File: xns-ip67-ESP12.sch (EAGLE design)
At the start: 86 parts, among them J1 DCJ0202

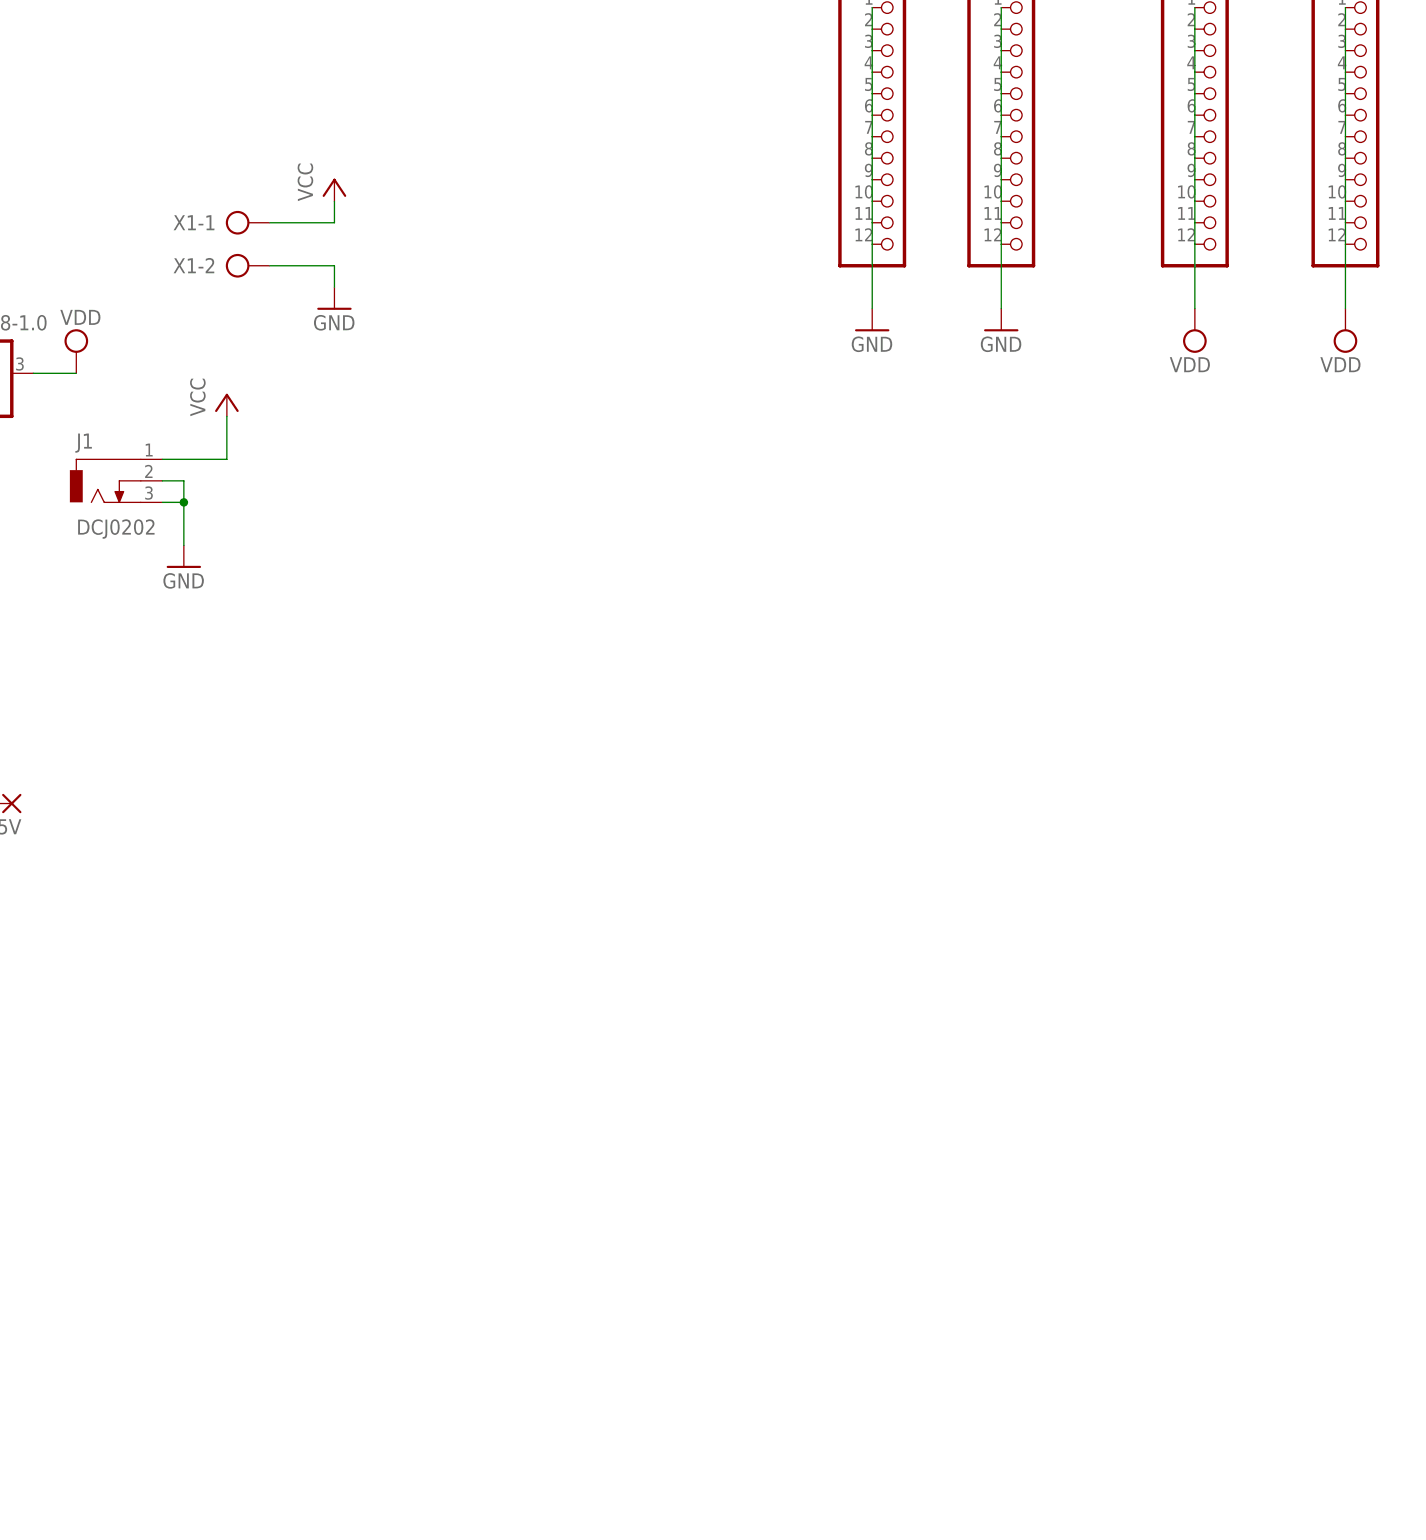
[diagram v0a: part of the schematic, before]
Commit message: Updated design
Added more wire pads on side of ESP
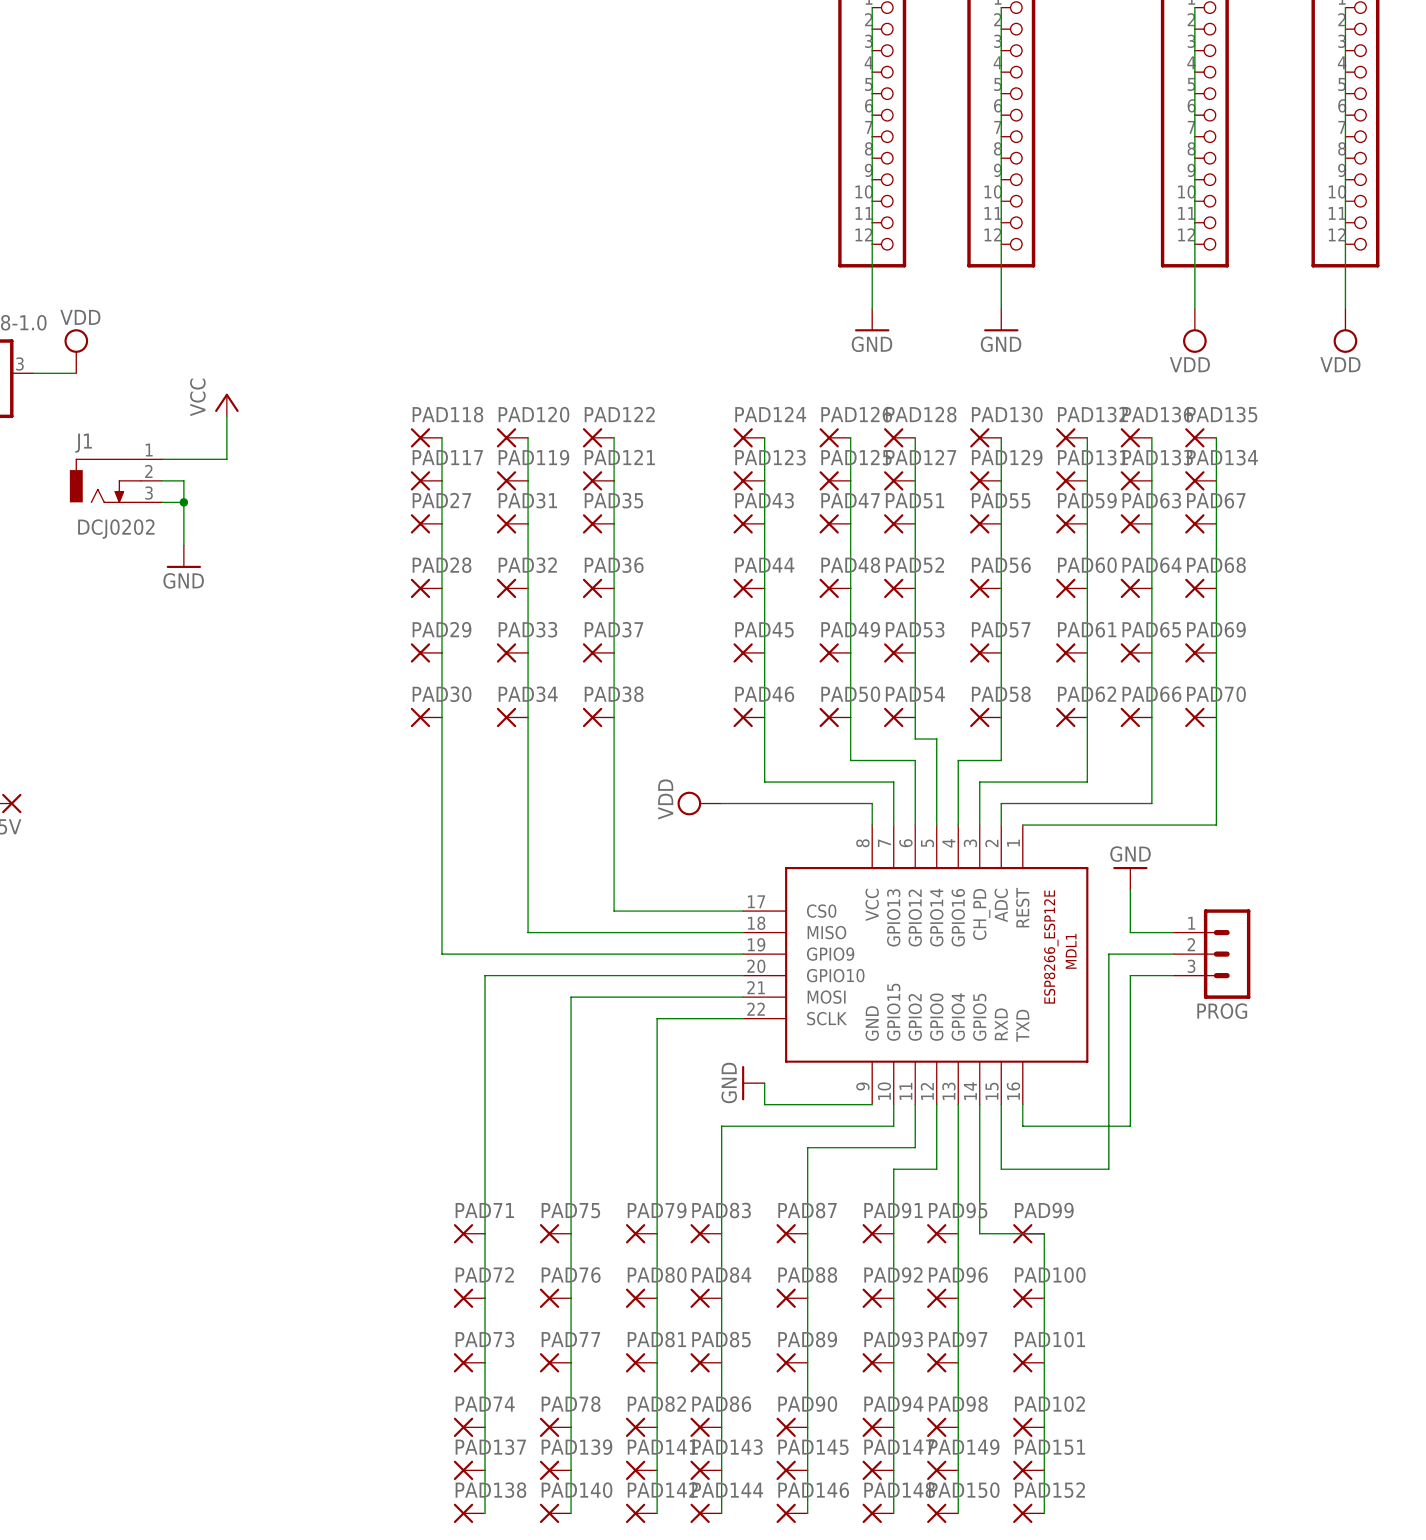
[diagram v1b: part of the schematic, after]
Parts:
- removed X1: (no value), con-ptr500:AK300/2
- added MDL1: (no value), ESP8266-ESP12E:ESP8266-12EESP8266-ESP12E
- added PAD100, PAD101, PAD102, PAD117, PAD118, PAD119, PAD120, PAD121, PAD122, PAD123, PAD124, PAD125, PAD126, PAD127, PAD128, PAD129, PAD130, PAD131, PAD132, PAD133, PAD134, PAD135, PAD136, PAD137, PAD138, PAD139, PAD140, PAD141, PAD142, PAD143, PAD144, PAD145, PAD146, PAD147, PAD148, PAD149, PAD150, PAD151, PAD152, PAD27, PAD28, PAD29, PAD30, PAD31, PAD32, PAD33, PAD34, PAD35, PAD36, PAD37, PAD38, PAD43, PAD44, PAD45, PAD46, PAD47, PAD48, PAD49, PAD50, PAD51, PAD52, PAD53, PAD54, PAD55, PAD56, PAD57, PAD58, PAD59, PAD60, PAD61, PAD62, PAD63, PAD64, PAD65, PAD66, PAD67, PAD68, PAD69, PAD70, PAD71, PAD72, PAD73, PAD74, PAD75, PAD76, PAD77, PAD78, PAD79, PAD80, PAD81, PAD82, PAD83, PAD84, PAD85, PAD86, PAD87, PAD88, PAD89, PAD90, PAD91, PAD92, PAD93, PAD94, PAD95, PAD96, PAD97, PAD98, PAD99: WIREPAD1,6/0,9, wirepad:WIREPAD1,6/0,9
- added PROG: (no value), con-lstb:MA03-1
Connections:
- new net N$1: MDL1.GPIO9, PAD117.P, PAD118.P, PAD27.P, PAD28.P, PAD29.P, PAD30.P
- new net N$10: MDL1.ADC, PAD133.P, PAD136.P, PAD63.P, PAD64.P, PAD65.P, PAD66.P
- new net N$11: MDL1.REST, PAD134.P, PAD135.P, PAD67.P, PAD68.P, PAD69.P, PAD70.P
- new net N$12: MDL1.GPIO10, PAD137.P, PAD138.P, PAD71.P, PAD72.P, PAD73.P, PAD74.P
- new net N$14: MDL1.SCLK, PAD141.P, PAD142.P, PAD79.P, PAD80.P, PAD81.P, PAD82.P
- new net N$15: MDL1.GPIO15, PAD143.P, PAD144.P, PAD83.P, PAD84.P, PAD85.P, PAD86.P
- new net N$16: MDL1.GPIO2, PAD145.P, PAD146.P, PAD87.P, PAD88.P, PAD89.P, PAD90.P
- new net N$17: MDL1.GPIO0, PAD147.P, PAD148.P, PAD91.P, PAD92.P, PAD93.P, PAD94.P
- new net N$18: MDL1.GPIO4, PAD149.P, PAD150.P, PAD95.P, PAD96.P, PAD97.P, PAD98.P
- new net N$19: MDL1.GPIO5, PAD100.P, PAD101.P, PAD102.P, PAD151.P, PAD152.P, PAD99.P
- new net N$2: MDL1.MISO, PAD119.P, PAD120.P, PAD31.P, PAD32.P, PAD33.P, PAD34.P
- new net N$20: MDL1.TXD, PROG.3
- new net N$3: MDL1.CS0, PAD121.P, PAD122.P, PAD35.P, PAD36.P, PAD37.P, PAD38.P
- new net N$4: MDL1.RXD, PROG.2
- new net N$5: MDL1.GPIO13, PAD123.P, PAD124.P, PAD43.P, PAD44.P, PAD45.P, PAD46.P
- new net N$6: MDL1.GPIO12, PAD125.P, PAD126.P, PAD47.P, PAD48.P, PAD49.P, PAD50.P
- new net N$70: MDL1.MOSI, PAD139.P, PAD140.P, PAD75.P, PAD76.P, PAD77.P, PAD78.P
- new net N$72: MDL1.GPIO14, PAD127.P, PAD128.P, PAD51.P, PAD52.P, PAD53.P, PAD54.P
- new net N$8: MDL1.GPIO16, PAD129.P, PAD130.P, PAD55.P, PAD56.P, PAD57.P, PAD58.P
- new net N$9: MDL1.CH_PD, PAD131.P, PAD132.P, PAD59.P, PAD60.P, PAD61.P, PAD62.P
- net GND: now also MDL1.GND, PROG.1; no longer X1-2.KL
- net VCC: no longer X1-1.KL
- net VDD: now also MDL1.VCC

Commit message: Change FTDI Header
Change FTDI Header
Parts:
- removed PROG: (no value), con-lstb:MA03-1
- added JP37: (no value), pinhead:PINHD-1X5
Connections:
- removed net N$20: MDL1.TXD, PROG.3
- new net N$13: JP37.4, MDL1.RXD
- new net N$7: JP23.1, JP23.2, JP23.3, JP23.4, JP23.5, JP23.6, JP23.7, JP23.8
- net GND: now also JP37.1; no longer PROG.1
- net N$4: now also JP37.5, MDL1.TXD; no longer MDL1.RXD, PROG.2
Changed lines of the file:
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@@
 <part name="PAD69" library="wirepad" deviceset="WIREPAD" device="1,6/0,9"/>
 <part name="PAD70" library="wirepad" deviceset="WIREPAD" device="1,6/0,9"/>
-<part name="PROG" library="con-lstb" deviceset="MA03-1" device=""/>
 <part name="PAD71" library="wirepad" deviceset="WIREPAD" device="1,6/0,9"/>
 <part name="PAD72" library="wirepad" deviceset="WIREPAD" device="1,6/0,9"/>
@@
 <part name="PAD151" library="wirepad" deviceset="WIREPAD" device="1,6/0,9"/>
 <part name="PAD152" library="wirepad" deviceset="WIREPAD" device="1,6/0,9"/>
+<part name="JP37" library="pinhead" deviceset="PINHD-1X5" device=""/>
 </parts>
 <sheets>
@@
 <attribute name="NAME" x="217.297" y="83.1342" size="1.778" layer="95"/>
 </instance>
-<instance part="PROG" gate="G$1" x="223.52" y="53.34" rot="R180"/>
 <instance part="PAD71" gate="G$1" x="132.08" y="20.32" smashed="yes">
 <attribute name="NAME" x="130.937" y="22.1742" size="1.778" layer="95"/>
@@
 <attribute name="NAME" x="196.977" y="-10.8458" size="1.778" layer="95"/>
 </instance>
+<instance part="JP37" gate="A" x="233.68" y="50.8"/>
 </instances>
 <busses>
@@
 <segment>
 <pinref part="GND3" gate="1" pin="GND"/>
-<wire x1="210.82" y1="60.96" x2="210.82" y2="55.88" width="0.1524" layer="91"/>
-<pinref part="PROG" gate="G$1" pin="1"/>
-<wire x1="210.82" y1="55.88" x2="215.9" y2="55.88" width="0.1524" layer="91"/>
+<wire x1="210.82" y1="60.96" x2="210.82" y2="58.42" width="0.1524" layer="91"/>
+<wire x1="210.82" y1="58.42" x2="223.52" y2="58.42" width="0.1524" layer="91"/>
+<wire x1="223.52" y1="58.42" x2="223.52" y2="55.88" width="0.1524" layer="91"/>
+<pinref part="JP37" gate="A" pin="1"/>
+<wire x1="223.52" y1="55.88" x2="231.14" y2="55.88" width="0.1524" layer="91"/>
 </segment>
 </net>
@@
 </segment>
 </net>
-<net name="N$4" class="0">
-<segment>
-<pinref part="MDL1" gate="G$1" pin="RXD"/>
-<wire x1="195.58" y1="35.56" x2="195.58" y2="27.94" width="0.1524" layer="91"/>
-<wire x1="195.58" y1="27.94" x2="208.28" y2="27.94" width="0.1524" layer="91"/>
-<wire x1="208.28" y1="27.94" x2="208.28" y2="53.34" width="0.1524" layer="91"/>
-<pinref part="PROG" gate="G$1" pin="2"/>
-<wire x1="208.28" y1="53.34" x2="215.9" y2="53.34" width="0.1524" layer="91"/>
-</segment>
-</net>
-<net name="N$20" class="0">
-<segment>
-<pinref part="PROG" gate="G$1" pin="3"/>
-<wire x1="215.9" y1="50.8" x2="210.82" y2="50.8" width="0.1524" layer="91"/>
-<wire x1="210.82" y1="50.8" x2="210.82" y2="33.02" width="0.1524" layer="91"/>
-<pinref part="MDL1" gate="G$1" pin="TXD"/>
-<wire x1="210.82" y1="33.02" x2="198.12" y2="33.02" width="0.1524" layer="91"/>
-<wire x1="198.12" y1="33.02" x2="198.12" y2="35.56" width="0.1524" layer="91"/>
-</segment>
-</net>
 <net name="N$72" class="0">
 <segment>
@@
 </segment>
 </net>
+<net name="N$7" class="0">
+<segment>
+<pinref part="JP23" gate="G$1" pin="1"/>
+<pinref part="JP23" gate="G$1" pin="2"/>
+<wire x1="322.58" y1="88.9" x2="322.58" y2="86.36" width="0.1524" layer="91"/>
+<pinref part="JP23" gate="G$1" pin="3"/>
+<wire x1="322.58" y1="86.36" x2="322.58" y2="83.82" width="0.1524" layer="91"/>
+<pinref part="JP23" gate="G$1" pin="4"/>
+<wire x1="322.58" y1="83.82" x2="322.58" y2="81.28" width="0.1524" layer="91"/>
+<pinref part="JP23" gate="G$1" pin="5"/>
+<wire x1="322.58" y1="81.28" x2="322.58" y2="78.74" width="0.1524" layer="91"/>
+<pinref part="JP23" gate="G$1" pin="6"/>
+<wire x1="322.58" y1="78.74" x2="322.58" y2="76.2" width="0.1524" layer="91"/>
+<pinref part="JP23" gate="G$1" pin="7"/>
+<wire x1="322.58" y1="76.2" x2="322.58" y2="73.66" width="0.1524" layer="91"/>
+<pinref part="JP23" gate="G$1" pin="8"/>
+<wire x1="322.58" y1="73.66" x2="322.58" y2="71.12" width="0.1524" layer="91"/>
+</segment>
+</net>
+<net name="N$4" class="0">
+<segment>
+<pinref part="MDL1" gate="G$1" pin="TXD"/>
+<wire x1="198.12" y1="35.56" x2="223.52" y2="35.56" width="0.1524" layer="91"/>
+<wire x1="223.52" y1="35.56" x2="223.52" y2="45.72" width="0.1524" layer="91"/>
+<pinref part="JP37" gate="A" pin="5"/>
+<wire x1="223.52" y1="45.72" x2="231.14" y2="45.72" width="0.1524" layer="91"/>
+</segment>
+</net>
+<net name="N$13" class="0">
+<segment>
+<pinref part="MDL1" gate="G$1" pin="RXD"/>
+<wire x1="195.58" y1="35.56" x2="195.58" y2="30.48" width="0.1524" layer="91"/>
+<wire x1="195.58" y1="30.48" x2="215.9" y2="30.48" width="0.1524" layer="91"/>
+<wire x1="215.9" y1="30.48" x2="215.9" y2="48.26" width="0.1524" layer="91"/>
+<pinref part="JP37" gate="A" pin="4"/>
+<wire x1="215.9" y1="48.26" x2="231.14" y2="48.26" width="0.1524" layer="91"/>
+</segment>
+</net>

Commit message: Routed and Gerb files
Routed and produced verb files
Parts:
- removed 5.5V, PAD1, PAD10, PAD100, PAD101, PAD102, PAD103, PAD104, PAD105, PAD106, PAD107, PAD108, PAD109, PAD11, PAD110, PAD111, PAD112, PAD113, PAD114, PAD115, PAD116, PAD117, PAD118, PAD119, PAD12, PAD120, PAD121, PAD122, PAD123, PAD124, PAD125, PAD126, PAD127, PAD128, PAD129, PAD13, PAD130, PAD131, PAD132, PAD133, PAD134, PAD135, PAD136, PAD137, PAD138, PAD139, PAD14, PAD140, PAD141, PAD142, PAD143, PAD144, PAD145, PAD146, PAD147, PAD148, PAD149, PAD15, PAD150, PAD151, PAD152, PAD16, PAD17, PAD18, PAD19, PAD2, PAD20, PAD21, PAD22, PAD23, PAD24, PAD25, PAD26, PAD27, PAD28, PAD29, PAD3, PAD30, PAD31, PAD32, PAD33, PAD34, PAD35, PAD36, PAD37, PAD38, PAD39, PAD4, PAD40, PAD41, PAD42, PAD43, PAD44, PAD45, PAD46, PAD47, PAD48, PAD49, PAD5, PAD50, PAD51, PAD52, PAD53, PAD54, PAD55, PAD56, PAD57, PAD58, PAD59, PAD6, PAD60, PAD61, PAD62, PAD63, PAD64, PAD65, PAD66, PAD67, PAD68, PAD69, PAD7, PAD70, PAD71, PAD72, PAD73, PAD74, PAD75, PAD76, PAD77, PAD78, PAD79, PAD8, PAD80, PAD81, PAD82, PAD83, PAD84, PAD85, PAD86, PAD87, PAD88, PAD89, PAD9, PAD90, PAD91, PAD92, PAD93, PAD94, PAD95, PAD96, PAD97, PAD98, PAD99: WIREPAD1,6/0,9, wirepad:WIREPAD1,6/0,9
- removed MDL1: (no value), ESP8266-ESP12E:ESP8266-12EESP8266-ESP12E
- added J10, J11, J12, J13, J18, J19, J2, J20, J21, J22, J23, J3, J4, J5, J6, J7, J8, J9: (no value), SparkFun-Connectors:M06NO_SILK_FEMALE_PTH
- added J14, J15, J16, J17: (no value), SparkFun-Connectors:M111X11_NO_SILK
- added J24: 5V, SparkFun-Connectors:M01PTH_NO_SILK_YES_STOP
- added J25, J26, J27, J28, J29, J30, J31, J32, J33, J34: (no value), SparkFun-Connectors:M07NO_SILK
- added X1: ESP-12E, microbuilder:ESP-12E
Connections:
- new net N$20: J22.1, J22.2, J22.3, J22.4, J22.5, J22.6
- new net N$52: J31.1, J31.2, J31.3, J31.4, J31.5, J31.6, J31.7
- new net N$54: J32.1, J32.2, J32.3, J32.4, J32.5, J32.6, J32.7
- new net N$56: J33.1, J33.2, J33.3, J33.4, J33.5, J33.6, J33.7
- new net N$58: J34.1, J34.2, J34.3, J34.4, J34.5, J34.6, J34.7
- new net N$71: J25.1, J25.2, J25.3, J25.4, J25.5, J25.6, J25.7
- new net N$73: J27.1, J27.2, J27.3, J27.4, J27.5, J27.6, J27.7
- new net N$74: J28.1, J28.2, J28.3, J28.4, J28.5, J28.6, J28.7
- new net N$75: J29.1, J29.2, J29.3, J29.4, J29.5, J29.6, J29.7
- new net N$76: J30.1, J30.2, J30.3, J30.4, J30.5, J30.6, J30.7
- net GND: now also J14.1, J14.10, J14.11, J14.2, J14.3, J14.4, J14.5, J14.6, J14.7, J14.8, J14.9, J16.1, J16.10, J16.11, J16.2, J16.3, J16.4, J16.5, J16.6, J16.7, J16.8, J16.9, X1.GND; no longer MDL1.GND, PAD1.P, PAD107.P, PAD108.P, PAD109.P, PAD110.P, PAD111.P, PAD13.P, PAD14.P, PAD15.P, PAD16.P, PAD17.P, PAD18.P, PAD19.P, PAD2.P, PAD25.P, PAD26.P, PAD3.P, PAD39.P, PAD4.P, PAD40.P, PAD5.P, PAD6.P
- net N$1: now also J2.1, J2.2, J2.3, J2.4, J2.5, J2.6, X1.GPIO13; no longer MDL1.GPIO9, PAD117.P, PAD118.P, PAD27.P, PAD28.P, PAD29.P, PAD30.P
- net N$10: now also J9.1, J9.2, J9.3, J9.4, J9.5, J9.6, X1.GPIO15; no longer MDL1.ADC, PAD133.P, PAD136.P, PAD63.P, PAD64.P, PAD65.P, PAD66.P
- net N$11: now also J10.1, J10.2, J10.3, J10.4, J10.5, J10.6, X1.GPIO2; no longer MDL1.REST, PAD134.P, PAD135.P, PAD67.P, PAD68.P, PAD69.P, PAD70.P
- net N$12: now also J11.1, J11.2, J11.3, J11.4, J11.5, J11.6, X1.GPIO0; no longer MDL1.GPIO10, PAD137.P, PAD138.P, PAD71.P, PAD72.P, PAD73.P, PAD74.P
- net N$13: now also X1.RXD; no longer MDL1.RXD
- net N$14: now also J12.1, J12.2, J12.3, J12.4, J12.5, J12.6, X1.GPIO4; no longer MDL1.SCLK, PAD141.P, PAD142.P, PAD79.P, PAD80.P, PAD81.P, PAD82.P
- net N$15: now also J13.1, J13.2, J13.3, J13.4, J13.5, J13.6, X1.GPIO5; no longer MDL1.GPIO15, PAD143.P, PAD144.P, PAD83.P, PAD84.P, PAD85.P, PAD86.P
- net N$16: now also J18.1, J18.2, J18.3, J18.4, J18.5, J18.6; no longer MDL1.GPIO2, PAD145.P, PAD146.P, PAD87.P, PAD88.P, PAD89.P, PAD90.P
- net N$17: now also J19.1, J19.2, J19.3, J19.4, J19.5, J19.6; no longer MDL1.GPIO0, PAD147.P, PAD148.P, PAD91.P, PAD92.P, PAD93.P, PAD94.P
- net N$18: now also J20.1, J20.2, J20.3, J20.4, J20.5, J20.6; no longer MDL1.GPIO4, PAD149.P, PAD150.P, PAD95.P, PAD96.P, PAD97.P, PAD98.P
- net N$19: now also J21.1, J21.2, J21.3, J21.4, J21.5, J21.6; no longer MDL1.GPIO5, PAD100.P, PAD101.P, PAD102.P, PAD151.P, PAD152.P, PAD99.P
- net N$2: now also J3.1, J3.2, J3.3, J3.4, J3.5, J3.6, X1.GPIO12; no longer MDL1.MISO, PAD119.P, PAD120.P, PAD31.P, PAD32.P, PAD33.P, PAD34.P
- net N$3: now also J4.1, J4.2, J4.3, J4.4, J4.5, J4.6, X1.GPIO14; no longer MDL1.CS0, PAD121.P, PAD122.P, PAD35.P, PAD36.P, PAD37.P, PAD38.P
- net N$4: now also X1.TXD; no longer MDL1.TXD
- net N$5: now also J5.1, J5.2, J5.3, J5.4, J5.5, J5.6, X1.GPIO16; no longer MDL1.GPIO13, PAD123.P, PAD124.P, PAD43.P, PAD44.P, PAD45.P, PAD46.P
- net N$6: now also J6.1, J6.2, J6.3, J6.4, J6.5, J6.6, X1.CH_PD; no longer MDL1.GPIO12, PAD125.P, PAD126.P, PAD47.P, PAD48.P, PAD49.P, PAD50.P
- net N$70: now also J23.1, J23.2, J23.3, J23.4, J23.5, J23.6; no longer MDL1.MOSI, PAD139.P, PAD140.P, PAD75.P, PAD76.P, PAD77.P, PAD78.P
- net N$72: now also J26.1, J26.2, J26.3, J26.4, J26.5, J26.6, J26.7; no longer MDL1.GPIO14, PAD127.P, PAD128.P, PAD51.P, PAD52.P, PAD53.P, PAD54.P
- net N$8: now also J7.1, J7.2, J7.3, J7.4, J7.5, J7.6, X1.ADC; no longer MDL1.GPIO16, PAD129.P, PAD130.P, PAD55.P, PAD56.P, PAD57.P, PAD58.P
- net N$9: now also J8.1, J8.2, J8.3, J8.4, J8.5, J8.6, X1.RESET; no longer MDL1.CH_PD, PAD131.P, PAD132.P, PAD59.P, PAD60.P, PAD61.P, PAD62.P
- net VCC: now also J24.1; no longer 5.5V.P
- net VDD: now also J15.1, J15.10, J15.11, J15.2, J15.3, J15.4, J15.5, J15.6, J15.7, J15.8, J15.9, J17.1, J17.10, J17.11, J17.2, J17.3, J17.4, J17.5, J17.6, J17.7, J17.8, J17.9, X1.VCC; no longer MDL1.VCC, PAD10.P, PAD103.P, PAD104.P, PAD105.P, PAD106.P, PAD11.P, PAD112.P, PAD113.P, PAD114.P, PAD115.P, PAD116.P, PAD12.P, PAD20.P, PAD21.P, PAD22.P, PAD23.P, PAD24.P, PAD41.P, PAD42.P, PAD7.P, PAD8.P, PAD9.P

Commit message: New board for Temp
New board for Temp logging with A7, Power lines is routed
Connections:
- net VCC: now also JP37.2
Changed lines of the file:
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@@
 <?xml version="1.0" encoding="utf-8"?>
 <!DOCTYPE eagle SYSTEM "eagle.dtd">
-<eagle version="7.7.0">
+<eagle version="8.0.2">
 <drawing>
 <settings>
@@
 <part name="J34" library="SparkFun-Connectors" deviceset="M07" device="NO_SILK"/>
 <part name="X1" library="microbuilder" deviceset="ESP-12E" device=""/>
+<part name="P+2" library="supply1" deviceset="VCC" device=""/>
 </parts>
 <sheets>
@@
 <instance part="U1" gate="G$1" x="50.8" y="93.98"/>
 <instance part="GND2" gate="1" x="165.1" y="38.1" rot="R270"/>
-<instance part="GND3" gate="1" x="210.82" y="63.5" rot="R180"/>
+<instance part="GND3" gate="1" x="215.9" y="66.04" rot="R180"/>
 <instance part="SUPPLY3" gate="G$1" x="160.02" y="71.12" rot="R90"/>
 <instance part="GND5" gate="1" x="-20.32" y="121.92"/>
@@
 <instance part="J34" gate="G$1" x="454.66" y="76.2"/>
 <instance part="X1" gate="G$1" x="187.96" y="53.34" rot="R270"/>
+<instance part="P+2" gate="VCC" x="223.52" y="66.04"/>
 </instances>
 <busses>
@@
 <wire x1="38.1" y1="93.98" x2="38.1" y2="99.06" width="0.1524" layer="91"/>
 <junction x="38.1" y="99.06"/>
+</segment>
+<segment>
+<pinref part="P+2" gate="VCC" pin="VCC"/>
+<wire x1="223.52" y1="63.5" x2="223.52" y2="53.34" width="0.1524" layer="91"/>
+<pinref part="JP37" gate="A" pin="2"/>
+<wire x1="223.52" y1="53.34" x2="231.14" y2="53.34" width="0.1524" layer="91"/>
 </segment>
 </net>
@@
 <segment>
 <pinref part="GND3" gate="1" pin="GND"/>
-<wire x1="210.82" y1="60.96" x2="210.82" y2="58.42" width="0.1524" layer="91"/>
-<wire x1="210.82" y1="58.42" x2="223.52" y2="58.42" width="0.1524" layer="91"/>
-<wire x1="223.52" y1="58.42" x2="223.52" y2="55.88" width="0.1524" layer="91"/>
+<wire x1="215.9" y1="63.5" x2="215.9" y2="55.88" width="0.1524" layer="91"/>
 <pinref part="JP37" gate="A" pin="1"/>
-<wire x1="223.52" y1="55.88" x2="231.14" y2="55.88" width="0.1524" layer="91"/>
-</segment>
-<segment>
+<wire x1="215.9" y1="55.88" x2="231.14" y2="55.88" width="0.1524" layer="91"/>
+</segment>
+<segment>
